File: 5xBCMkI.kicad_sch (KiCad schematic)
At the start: 5 parts, among them Q1 OSP120N04T

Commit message: ADDED all LCSC part numbers and footprints. FIXED schematic (and model) to use a smaller range of resistor and capacitor values to increase cost efficiency, at the expense of control system performance. TODO begin designing PCB.
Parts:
- C6: renamed from C5; footprint (none) -> Capacitor_THT:CP_Radial_D10.0mm_P5.00mm
- C7: renamed from C6; footprint (none) -> PCM_Capacitor_THT_AKL:C_Axial_L3.0mm_D2.3mm_P7.50mm_Horizontal
- D1: footprint (none) -> Diode_THT:D_DO-41_SOD81_P10.16mm_Horizontal
- L1: footprint (none) -> Inductor_THT:L_Radial_D12.0mm_P5.00mm_Fastron_11P
- Q1: footprint Package_TO_SOT_THT:TO-220-3_Vertical -> PCM_Package_TO_SOT_THT_AKL:TO-220-3_Vertical_GDS; LCSC Part # (none) -> C51949596
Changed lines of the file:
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@@
+	)
+	(junction
+		(at 125.73 86.36)
+		(diameter 0)
+		(color 0 0 0 0)
 	)
 	(junction
@@
 	(wire
 		(pts
+			(xy 138.43 80.01) (xy 138.43 86.36)
+		)
+		(stroke
+			(width 0)
+			(type default)
+		)
+	)
+	(wire
+		(pts
 			(xy 171.45 86.36) (xy 171.45 91.44)
 		)
@@
 	(wire
 		(pts
-			(xy 123.19 86.36) (xy 128.27 86.36)
+			(xy 123.19 86.36) (xy 125.73 86.36)
 		)
 		(stroke
@@
 	(wire
 		(pts
+			(xy 125.73 86.36) (xy 128.27 86.36)
+		)
+		(stroke
+			(width 0)
+			(type default)
+		)
+	)
+	(wire
+		(pts
 			(xy 138.43 86.36) (xy 143.51 86.36)
+		)
+		(stroke
+			(width 0)
+			(type default)
+		)
+	)
+	(wire
+		(pts
+			(xy 125.73 82.55) (xy 125.73 86.36)
 		)
 		(stroke
@@
 			)
 			(justify left)
+		)
+	)
+	(netclass_flag ""
+		(length 2.54)
+		(shape diamond)
+		(at 154.94 86.36 0)
+		(fields_autoplaced yes)
+		(effects
+			(font
+				(size 1.27 1.27)
+			)
+			(justify left bottom)
+		)
+		(property "Netclass" "BoostConvPower"
+			(at 156.1465 83.82 0)
+			(effects
+				(font
+					(size 1.27 1.27)
+				)
+				(justify left)
+			)
+		)
+		(property "Component Class" ""
+			(at -6.35 6.35 0)
+			(effects
+				(font
+					(size 1.27 1.27)
+					(italic yes)
+				)
+			)
+		)
+	)
+	(netclass_flag ""
+		(length 2.54)
+		(shape diamond)
+		(at 138.43 80.01 0)
+		(fields_autoplaced yes)
+		(effects
+			(font
+				(size 1.27 1.27)
+			)
+			(justify left bottom)
+		)
+		(property "Netclass" "BoostConvPower"
+			(at 139.6365 77.47 0)
+			(effects
+				(font
+					(size 1.27 1.27)
+				)
+				(justify left)
+			)
+		)
+		(property "Component Class" ""
+			(at -39.37 12.7 0)
+			(effects
+				(font
+					(size 1.27 1.27)
+					(italic yes)
+				)
+			)
+		)
+	)
+	(netclass_flag ""
+		(length 2.54)
+		(shape diamond)
+		(at 125.73 82.55 0)
+		(fields_autoplaced yes)
+		(effects
+			(font
+				(size 1.27 1.27)
+			)
+			(justify left bottom)
+		)
+		(property "Netclass" "BoostConvPower"
+			(at 124.5235 80.01 0)
+			(effects
+				(font
+					(size 1.27 1.27)
+				)
+				(justify right)
+			)
+		)
+		(property "Component Class" ""
+			(at 411.48 19.05 0)
+			(effects
+				(font
+					(size 1.27 1.27)
+					(italic yes)
+				)
+				(justify left)
+			)
 		)
 	)
@@
 		(dnp no)
 		(fields_autoplaced yes)
-		(property "Reference" "#PWR019"
+		(property "Reference" "#PWR021"
 			(at 138.43 109.22 0)
 			(effects
@@
 			(project ""
 				(path "/fde5ddde-7ac3-4123-99a9-b1b8b10c441e/218378dc-6e1f-4dbe-8817-2cd6f3f5419d"
-					(reference "#PWR019")
+					(reference "#PWR021")
 					(unit 1)
 				)
@@
 		(dnp no)
 		(fields_autoplaced yes)
-		(property "Reference" "C5"
+		(property "Reference" "C6"
 			(at 162.56 94.2339 0)
 			(effects
@@
 			)
 		)
-		(property "Footprint" ""
+		(property "Footprint" "Capacitor_THT:CP_Radial_D10.0mm_P5.00mm"
 			(at 158.75 95.25 0)
 			(effects
@@
 			)
 		)
-		(property "Datasheet" ""
+		(property "Datasheet" "~"
 			(at 158.75 95.25 0)
 			(effects
@@
 			(project ""
 				(path "/fde5ddde-7ac3-4123-99a9-b1b8b10c441e/218378dc-6e1f-4dbe-8817-2cd6f3f5419d"
-					(reference "C5")
+					(reference "C6")
 					(unit 1)
 				)
@@
 		(dnp no)
 		(fields_autoplaced yes)
-		(property "Reference" "C6"
+		(property "Reference" "C7"
 			(at 175.26 93.9799 0)
 			(effects
@@
 			)
 		)
-		(property "Footprint" ""
+		(property "Footprint" "PCM_Capacitor_THT_AKL:C_Axial_L3.0mm_D2.3mm_P7.50mm_Horizontal"
 			(at 172.4152 99.06 0)
 			(effects
@@
 			(project ""
 				(path "/fde5ddde-7ac3-4123-99a9-b1b8b10c441e/218378dc-6e1f-4dbe-8817-2cd6f3f5419d"
-					(reference "C6")
+					(reference "C7")
 					(unit 1)
 				)
@@
 			)
 		)
-		(property "Footprint" ""
+		(property "Footprint" "Diode_THT:D_DO-41_SOD81_P10.16mm_Horizontal"
 			(at 147.32 86.36 0)
 			(effects
@@
 			)
 		)
-		(property "Footprint" ""
+		(property "Footprint" "Inductor_THT:L_Radial_D12.0mm_P5.00mm_Fastron_11P"
 			(at 132.08 86.36 0)
 			(effects
@@
 			)
 		)
-		(property "Footprint" "Package_TO_SOT_THT:TO-220-3_Vertical"
+		(property "Footprint" "PCM_Package_TO_SOT_THT_AKL:TO-220-3_Vertical_GDS"
 			(at 139.446 110.49 0)
 			(effects
@@
 			(effects
 				(font
+					(size 1.27 1.27)
+				)
+				(hide yes)
+			)
+		)
+		(property "LCSC Part #" "C51949596"
+			(at 135.89 95.25 0)
+			(effects
+				(font

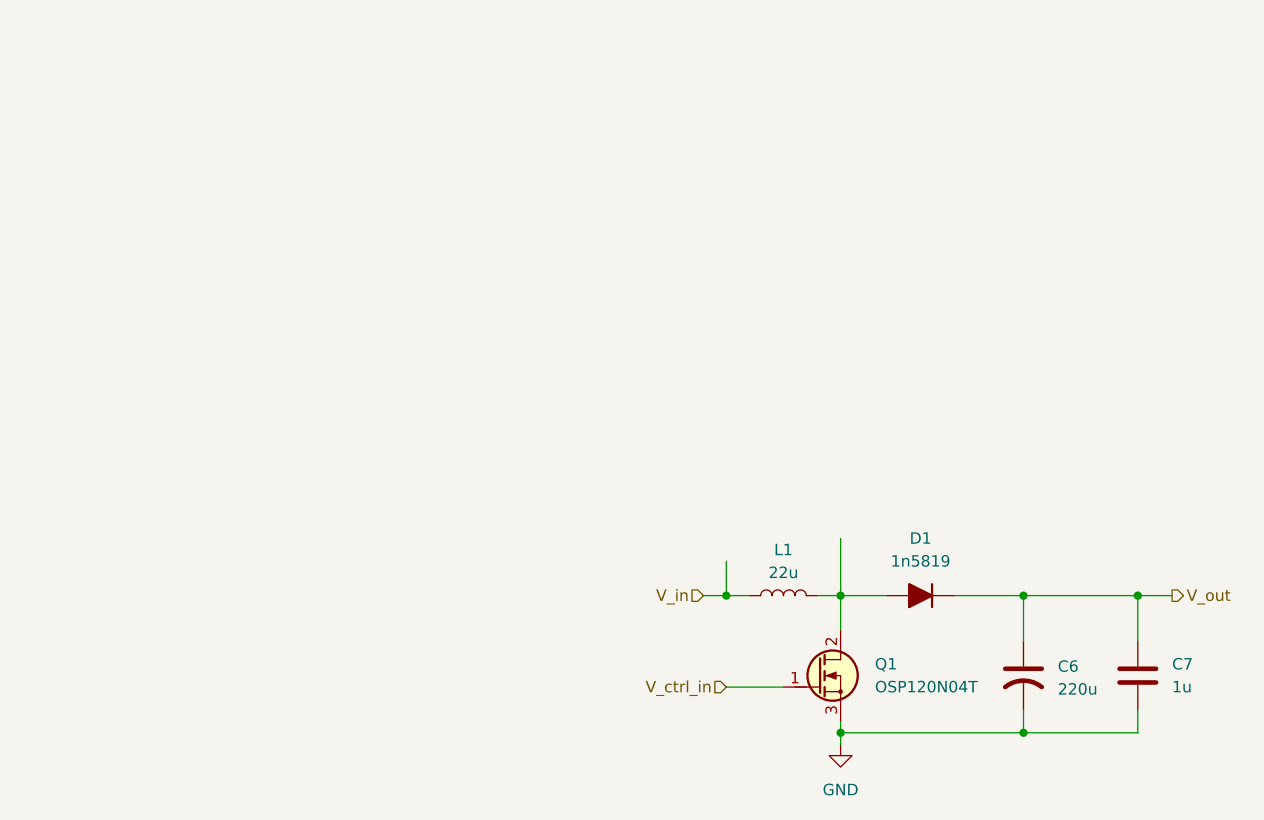
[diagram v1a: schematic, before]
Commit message: Finalized design files for assembly and organized BOM.
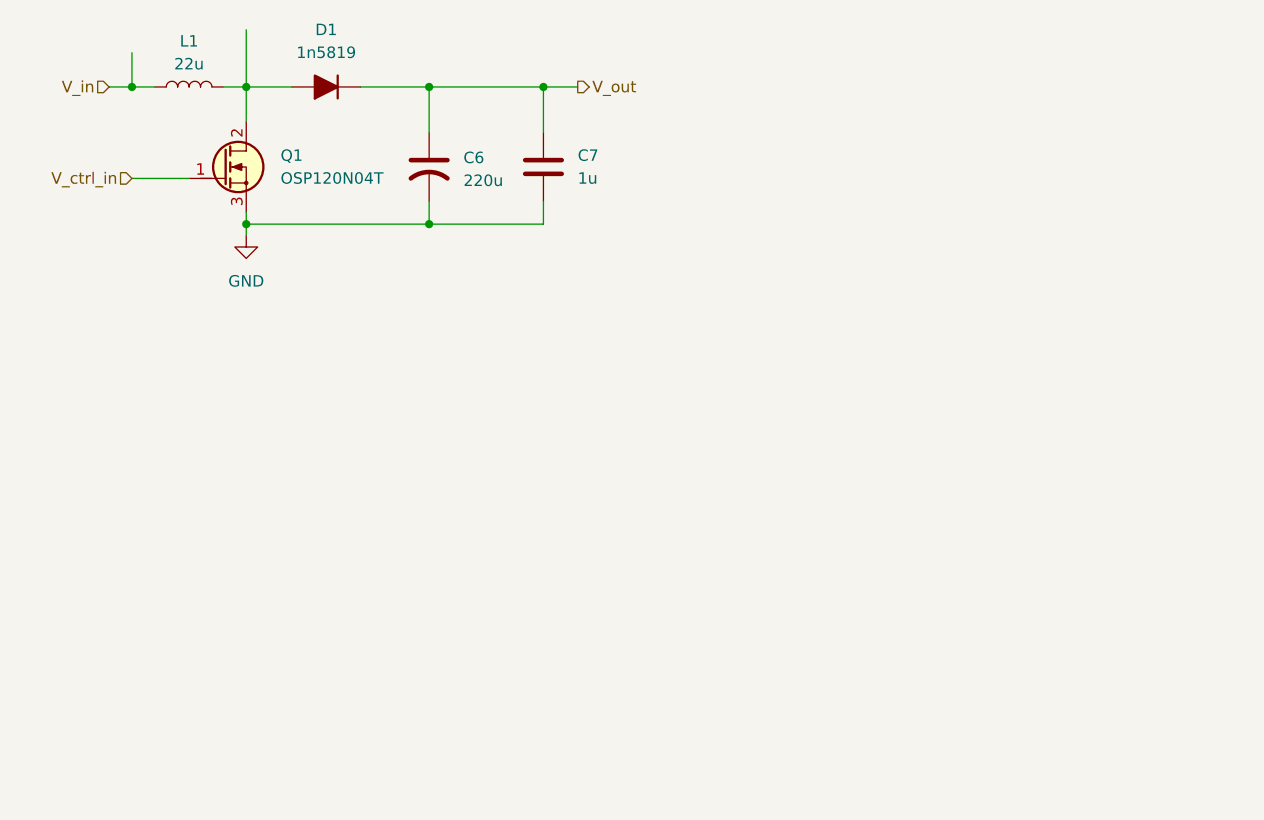
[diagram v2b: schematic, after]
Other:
- moved on the sheet: C6, C7, D1, L1, Q1
